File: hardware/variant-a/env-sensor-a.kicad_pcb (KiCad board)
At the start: 4 copper layers, 30 x 34 mm, 58 parts, among them J1 USB-C 16P, J2 JST-PH 2P, SW1 SW_PROV, U1 ESP32-C6-MINI-1-N4, U2 SHT45-AD1F, U3 TPS62840DLC, U4 BQ24074RGTR, U5 USBLC6-2SC6

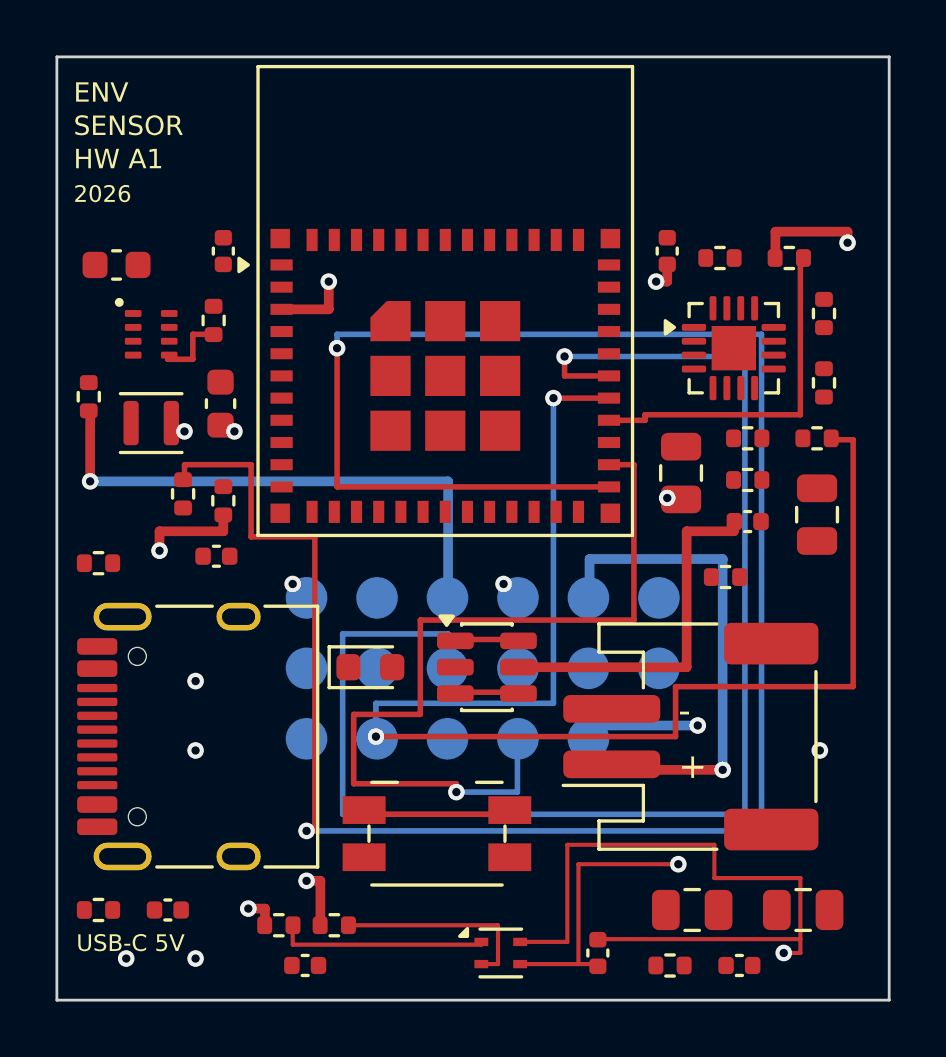
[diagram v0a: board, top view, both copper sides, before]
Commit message: chore(hw): regenerate both boards and previews after review fixes
Emit shared electrical corrections, validated routing and strengthened rules. Development allowances: A54/B58 unrouted and A6/B10 warnings per e584c6a; zero errors and parity differences. Preserve native KiCad SVG formatting. These are draft boards.
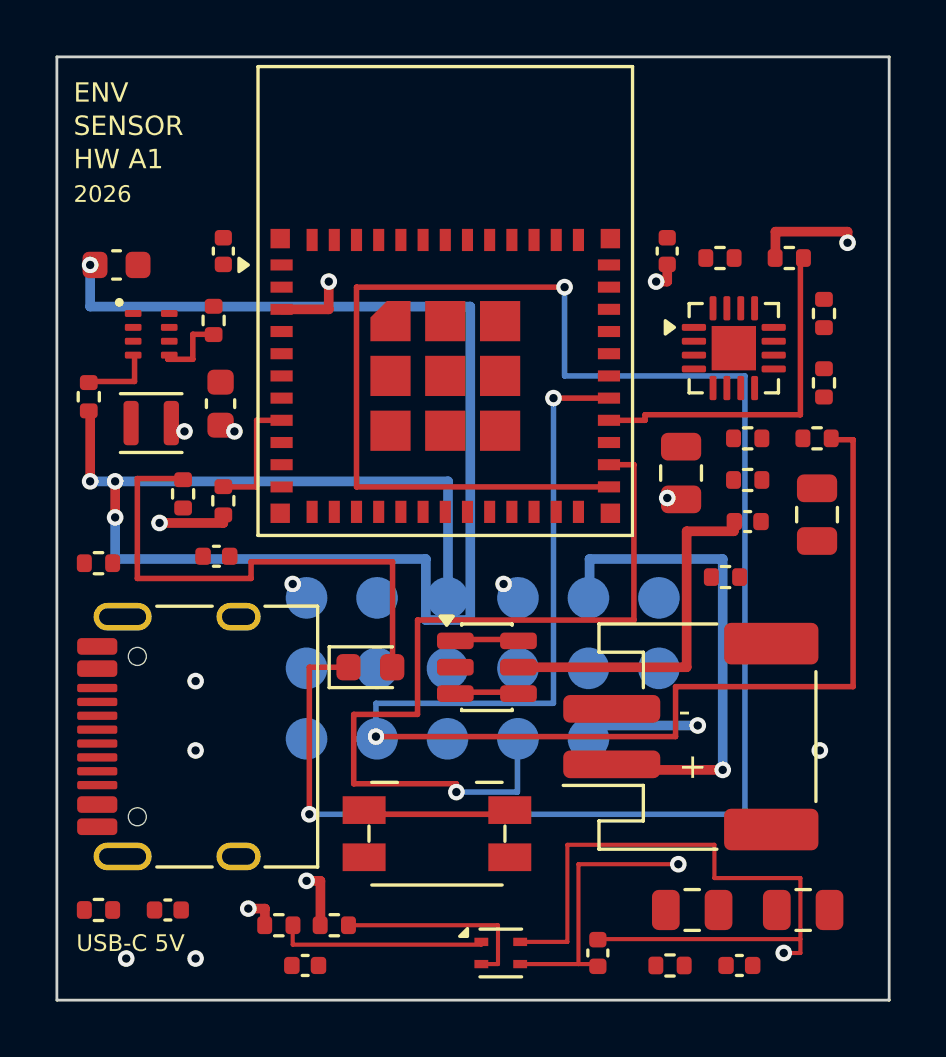
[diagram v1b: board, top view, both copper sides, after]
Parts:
- R6: value 52k3 1% -> 267k 1%
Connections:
- D1 pad 1: LED_A -> LED_N
- D1 pad 2: GND -> LED_A
- R2 pad 1: LED_A -> +3V0
- R2 pad 2: LED_N -> LED_A
- R5 pad 2: VSYS -> EN_REG
- U3 pad 4: VSYS -> EN_REG
- U4 pad 14: GND -> unconnected-(U4-TMR-Pad14)
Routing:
- net UART_RX: track 51.3 -> 0.00 mm, vias 1 -> 0
- net VSYS: track 19.7 -> 64.2 mm, vias 1 -> 4
- net LED_A: track 0.00 -> 18.9 mm
- net LED_N: track 83.6 -> 71.7 mm
- net EN: track 0.00 -> 4.50 mm
- net EN_REG: track 0.00 -> 2.60 mm
- net +3V0: track 27.6 -> 26.6 mm

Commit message: chore(hw): regenerate both variants for power architecture
Regenerate the shared schematic, both PCB layouts, symbol library, BOM, netlist, enclosure parameters, cost reports and floorplan previews from the updated electrical platform.

Record the reviewed KiCad 10 development budget: zero errors and parity differences, with 59 unrouted items on A and 60 on B. These artifacts remain non-release drafts.
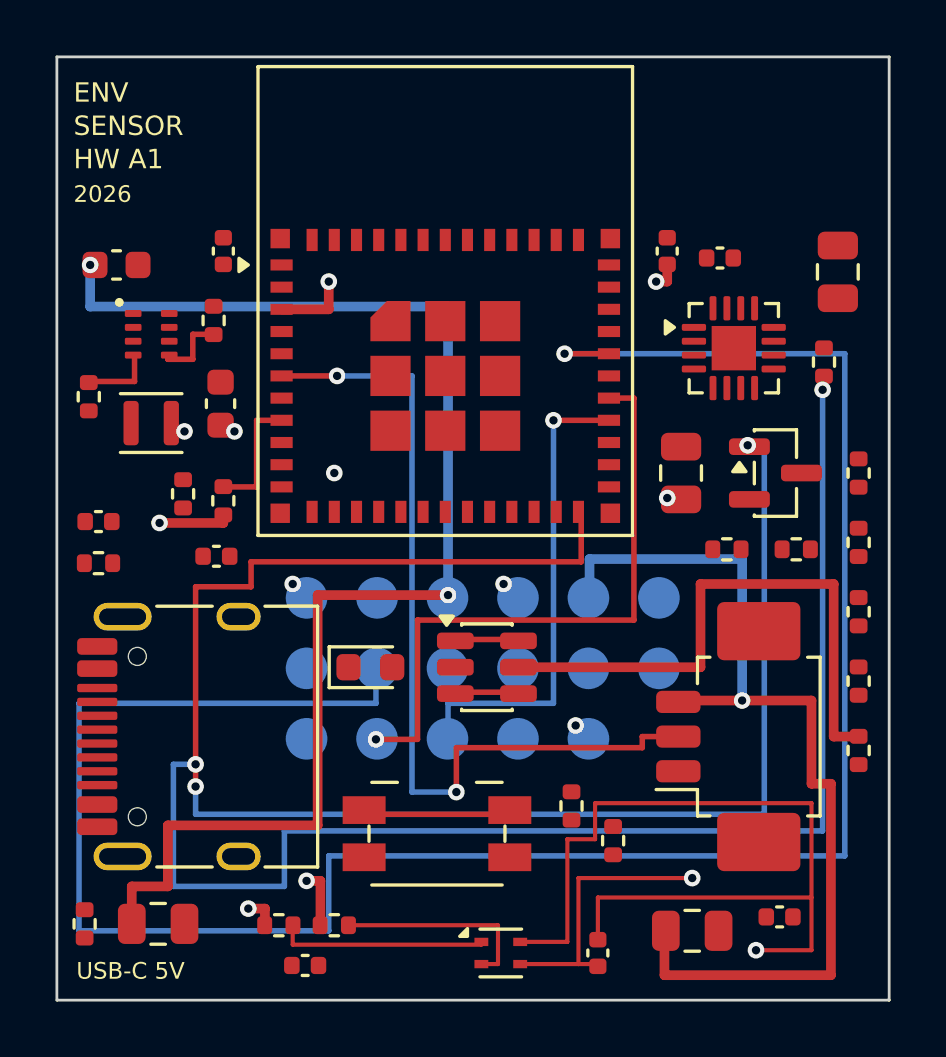
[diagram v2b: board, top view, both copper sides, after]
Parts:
- added Q1: 2N7002, sensorly:SOT-23, F.Cu at (125.9, 75.0)
- added R18: 47k 1%, sensorly:R_0402_1005Metric, F.Cu at (128.9, 85.0)
- J2: value JST-PH 2P -> Molex PicoBlade 3P; footprint sensorly:JST_PH_S2B-PH-SM4-TB_1x02-1MP_P2.00mm_Horizontal -> sensorly:Molex_PicoBlade_53261-0371_1x03-1MP_P1.25mm_Horizontal
- R11: value 3k09 1% -> 8k00 1%
- R13: value 3k57 1% -> 4k42 1%
- R7: value 10k 1% -> 100k 1%
- moved C10 19.3 mm to (103.7, 91.2)
- moved C14 14.2 mm to (101.5, 76.8)
- moved R9 10.6 mm to (128.9, 77.5), turned to 90 degrees
- moved R14 10.3 mm to (120.0, 88.2), turned to 90 degrees
- moved C12 9.55 mm to (123.9, 67.2)
- moved C9 8.78 mm to (128.2, 67.8)
- moved R11 8.56 mm to (126.7, 77.8), turned to 0 degrees
- moved R12 8.34 mm to (128.9, 80.0)
- moved R13 8.28 mm to (128.9, 82.5), turned to 90 degrees
- moved R15 6.76 mm to (118.5, 87.0), turned to 90 degrees
- moved R7 5.30 mm to (127.7, 71.0), turned to 90 degrees
- moved R10 5.15 mm to (124.2, 77.8)
- moved R8 4.19 mm to (128.9, 75.0), turned to 90 degrees
- moved C11 4.07 mm to (122.9, 91.5)
- moved C13 2.27 mm to (126.0, 91.0)
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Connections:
- J2 pad 1: VBAT -> GND
- J2 pad 2: GND -> PACK_TS
- J2 pad MP: GND -> unconnected-(J2-MountPin-PadMP)
- R7 pad 1: TS -> CHARGE_ENABLE
- R8 pad 1: VBUS -> USB_ISEL
- R8 pad 2: EN2 -> GND
- U1 pad 24: unconnected-(U1-IO18-Pad24) -> CHARGE_ENABLE
- U1 pad 27: unconnected-(U1-IO21-Pad27) -> USB_ISEL
- U1 pad 6: unconnected-(U1-IO3-Pad6) -> PACK_TS
- U4 pad 1: TS -> PACK_TS
- U4 pad 4: GND -> CHARGE_EN_N
- U4 pad 5: EN2 -> GND
- U4 pad 6: GND -> USB_ISEL
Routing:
- net CHARGE_ENABLE: track 0.00 -> 106.3 mm, vias 0 -> 4
- net UART_TX: track 0.00 -> 80.3 mm, vias 0 -> 1
- net LED_N: track 71.7 -> 0.00 mm, vias 2 -> 0
- net PACK_TS: track 0.00 -> 31.3 mm, vias 0 -> 2
- net TEST_MODE: track 30.6 -> 0.00 mm, vias 1 -> 0
- net CHG_N: track 49.3 -> 22.5 mm, vias 2 -> 1
- net LED_A: track 18.9 -> 0.00 mm
- net VBAT: track 18.0 -> 35.0 mm
- net VSYS: track 64.2 -> 48.2 mm, vias 4 -> 2
- net VBUS: track 13.0 -> 20.8 mm
- net PG_N: track 12.9 -> 17.3 mm, vias 0 -> 1
- net +3V0: track 26.6 -> 22.7 mm, vias 11 -> 10
- net GND: track 30.8 -> 34.0 mm, vias 8 -> 4
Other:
- board text added: "- T +"
- board text removed: "+"
- board text removed: "-"

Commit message: chore(hw): regenerate the controlled prototype checkpoint
Regenerate shared schematic/BOM/netlist, both PCB projects/rules and floorplan SVGs from the electrical, library and routing corrections in 3c343e2, 135b78b, d863f52, 7802bdf, 0852837 and 7206b19. Preserve R21 DNP and the common A/B electrical platform.

Fresh KiCad 10.0.6: zero ERC violations; both boards have zero DRC errors, warnings and schematic parity differences, with no ignored checks. Development routing exception: A59/B52 unconnected items remain, explicitly recorded in the budget; all old warning allowances are removed. Prototype and product manufacturing gates still require complete routing and real qualification evidence. Full committed-source pipeline follows before push.
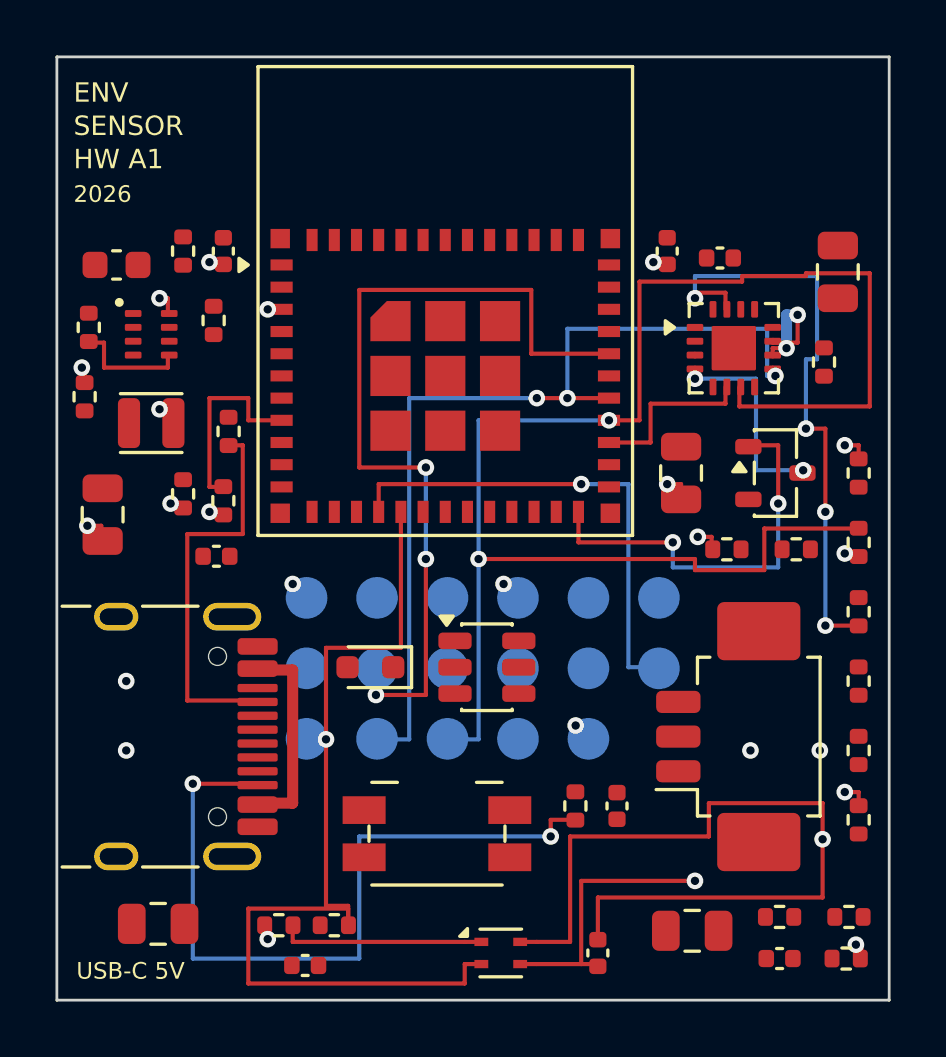
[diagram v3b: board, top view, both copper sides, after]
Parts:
- added R19: 100k 1%, sensorly:R_0402_1005Metric, F.Cu at (128.4, 92.5)
- added R20: 100k 1%, sensorly:R_0402_1005Metric, F.Cu at (128.9, 87.5)
- added R21: 0R, sensorly:R_0402_1005Metric, F.Cu at (104.5, 67.0)
- added R22: 10k 1%, sensorly:R_0402_1005Metric, F.Cu at (101.0, 72.2)
- C1: value 22uF/6.3V X5R -> 10uF/16V X5R
- C10, C11: value 10uF/6.3V X5R -> 10uF/16V X5R
- C3, C4: value 1uF/16V X7R -> 1uF/16V X5R
- C8: value 10uF/6.3V X5R -> 10uF/16V X5R; footprint sensorly:C_0603_1608Metric -> sensorly:C_0805_2012Metric
- D1: footprint sensorly:LED_0603_1608Metric -> sensorly:Kingbright_KP1608SGC
- L1: footprint sensorly:L_Murata_DFE201610P -> sensorly:L_Murata_DFE201612E
- Q1: footprint sensorly:SOT-23 -> sensorly:Onsemi_CASE318_SOT23
- R11: value 8k00 1% -> 8k06 1%
- TP10: value USB_DP -> USB_D_P
- TP11: value USB_DM -> USB_D_N
- TP7: value BTN_PROV -> BOOT_N
- U4: footprint sensorly:VQFN-16-1EP_3x3mm_P0.5mm_EP1.6x1.6mm -> sensorly:TI_RGT0016B_VQFN16_3x3mm
- U5: footprint sensorly:SOT-23-6 -> sensorly:ST_USBLC6_SOT23_6
- moved C14 21.3 mm to (120.2, 87.0), turned to 90 degrees
- moved R17 18.2 mm to (118.7, 87.0)
- moved R15 10.8 mm to (128.6, 91.0), turned to 0 degrees
- moved R16 6.68 mm to (106.2, 73.5), turned to 90 degrees
- moved R14 6.60 mm to (126.0, 91.0), turned to 0 degrees
- moved C8 5.84 mm to (101.7, 76.5)
- moved R5 5.27 mm to (105.7, 69.5)
- moved R6 4.51 mm to (101.2, 69.8)
- moved J1 2.31 mm to (103.2, 84.5), turned to 270 degrees
- moved C13 1.50 mm to (126.0, 92.5)
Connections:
- net USB_DM renamed USB_D_N
- net USB_DP renamed USB_D_P
- D1 pad 1: LED_N -> LED_A
- D1 pad 2: LED_A -> LED_N
- R8 pad 2: GND -> +3V0
- TP7 pad 1: BTN_PROV -> BOOT_N
- U1 pad 13: unconnected-(U1-IO1-Pad13) -> BTN_PROV
- U1 pad 19: unconnected-(U1-IO14-Pad19) -> USB_EN2
- U1 pad 22: unconnected-(U1-IO8-Pad22) -> BOOT_MODE_H
- U1 pad 23: BTN_PROV -> BOOT_N
- U1 pad 6: PACK_TS -> PACK_TS_SENSE
- U4 pad 5: GND -> USB_EN2
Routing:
- net CHARGE_ENABLE: track 106.3 -> 14.7 mm, vias 4 -> 2
- net UART_TX: track 80.3 -> 31.1 mm, vias 1 -> 3
- net VSYS: track 48.2 -> 4.40 mm
- net PG_N: track 17.3 -> 57.8 mm, vias 1 -> 2
- net VBAT: track 35.0 -> 0.10 mm, vias 1 -> 0
- net PACK_TS: track 31.3 -> 0.00 mm, vias 2 -> 0
- net SCL: track 7.40 -> 35.1 mm, vias 0 -> 1
- net CC2: track 0.00 -> 27.4 mm, vias 0 -> 2
- net ITERM: track 0.00 -> 22.0 mm, vias 0 -> 4
- net SDA: track 7.60 -> 25.1 mm, vias 0 -> 1
- net CC1: track 0.00 -> 14.2 mm
- net VBUS: track 20.8 -> 7.60 mm
- net CHG_N: track 22.5 -> 32.8 mm, vias 1 -> 3
- net CHARGE_EN_N: track 0.00 -> 7.60 mm, vias 0 -> 2
- net USB_ISEL: track 0.00 -> 6.20 mm
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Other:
- board text added: "J2 1- 2T 3+"
- board text removed: "- T +"

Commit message: build(boardgen): regenerate reviewed local power layouts
Regenerate both boards, rule areas, floorplan SVGs and enclosure parameters from 3109ac3. Preserve zero DRC errors/warnings/parity with A56/B49 unfinished connections; outputs remain draft engineering artifacts.
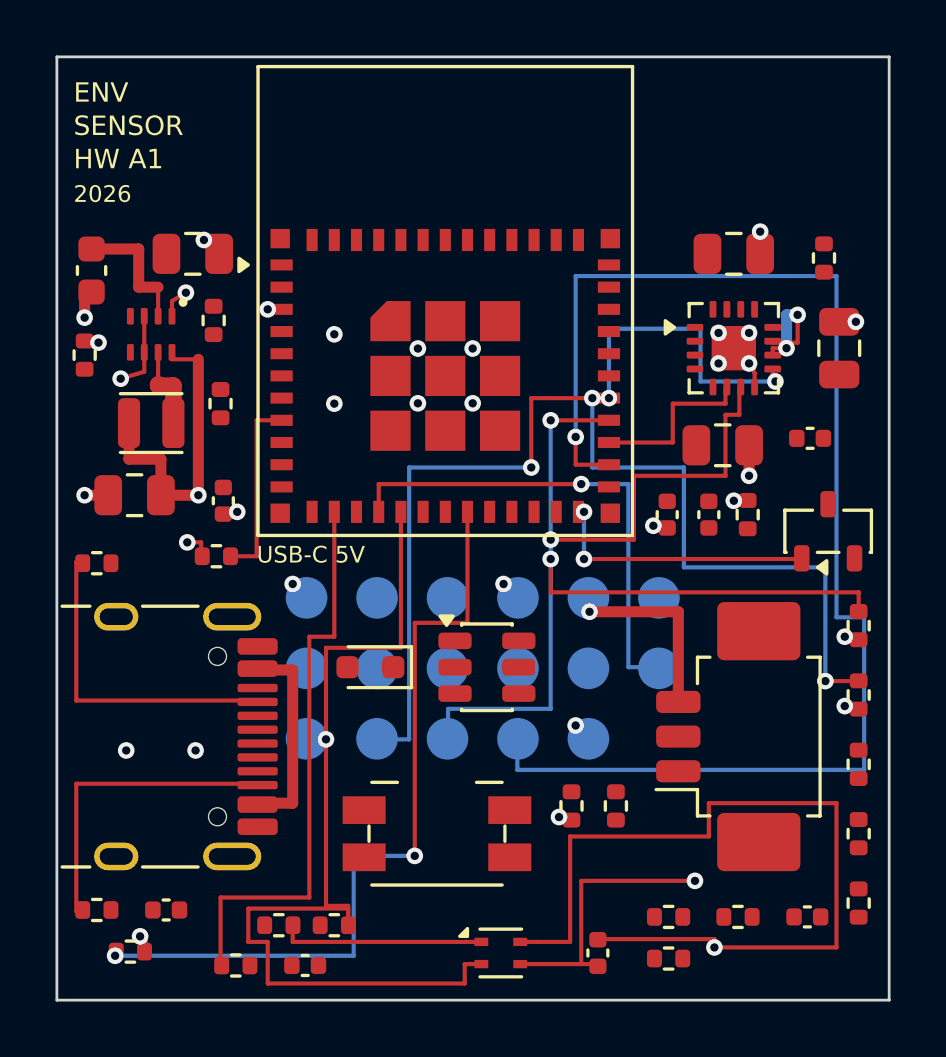
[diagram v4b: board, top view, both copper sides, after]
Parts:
- moved C10 32.1 mm to (128.2, 70.5), turned to 90 degrees
- moved R21 30.9 mm to (122.0, 92.5), turned to 0 degrees
- moved R20 26.7 mm to (102.7, 92.2), turned to 0 degrees
- moved R19 22.0 mm to (106.5, 92.8)
- moved C1 19.3 mm to (104.9, 67.1), turned to 180 degrees
- moved R2 18.0 mm to (118.5, 87.0)
- moved C4 17.8 mm to (123.5, 76.5), turned to 90 degrees
- moved R17 17.7 mm to (101.4, 90.8), turned to 0 degrees
- moved C11 17.5 mm to (124.0, 74.0)
- moved C14 16.7 mm to (103.9, 90.8), turned to 0 degrees
- moved R12 11.2 mm to (120.2, 87.0)
- moved C3 9.50 mm to (122.0, 76.5)
- moved C2 9.00 mm to (106.0, 76.0)
- moved R11 8.07 mm to (128.9, 85.5), turned to 90 degrees
- moved C12 7.27 mm to (127.2, 73.8)
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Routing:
- net TEST_MODE: track 0.10 -> 49.8 mm, vias 0 -> 1
- net UART_TX: track 31.1 -> 0.00 mm, vias 3 -> 0
- net USB_EN2: track 0.00 -> 28.7 mm, vias 0 -> 2
- net ITERM: track 22.0 -> 0.00 mm, vias 4 -> 0
- net BTN_PROV: track 0.00 -> 20.5 mm
- net CHG_N: track 32.8 -> 51.5 mm, vias 3 -> 5
- net CC2: track 27.4 -> 11.3 mm, vias 2 -> 0
- net PG_N: track 57.8 -> 42.6 mm, vias 2 -> 3
- net GND: track 30.9 -> 41.9 mm, vias 7 -> 22
- net CHARGE_EN_N: track 7.60 -> 0.00 mm, vias 2 -> 0
- net VBAT: track 0.10 -> 7.00 mm, vias 0 -> 1
- net +3V0: track 23.3 -> 29.5 mm, vias 18 -> 14
- net CHARGE_ENABLE: track 14.7 -> 9.50 mm
- net VSYS: track 4.40 -> 9.23 mm
- net VSET: track 4.20 -> 0.00 mm
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
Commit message: build(boardgen): regenerate local charger power routes
Regenerate both boards and model SVGs from the preceding charger-bypass source change. A47/B45 unconnected items remain explicitly recorded.
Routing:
- net EN: track 6.70 -> 62.4 mm, vias 0 -> 3
- net UART_TX: track 0.00 -> 40.1 mm, vias 0 -> 3
- net ILIM: track 0.00 -> 23.7 mm, vias 0 -> 2
- net LED_N: track 0.00 -> 21.3 mm, vias 0 -> 2
- net TEST_MODE: track 49.8 -> 29.6 mm
- net PACK_TS: track 0.00 -> 17.9 mm, vias 0 -> 2
- net CHARGE_ENABLE: track 9.50 -> 20.6 mm, vias 2 -> 4
- net CHG_N: track 51.5 -> 45.2 mm, vias 5 -> 4
- net VBUS: track 7.60 -> 11.3 mm
- net PG_N: track 42.6 -> 45.3 mm
- net USB_ISEL: track 6.20 -> 8.60 mm
- net USB_EN2: track 28.7 -> 29.9 mm
- net VBAT: track 7.00 -> 6.20 mm, vias 1 -> 0
- net VSYS: track 9.23 -> 9.22 mm, vias 2 -> 0

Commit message: build(boardgen): regenerate regulator control routing
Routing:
- net BOOT_MODE_H: track 0.40 -> 21.3 mm, vias 0 -> 4
- net VSET: track 0.00 -> 9.69 mm, vias 0 -> 2
- net EN_REG: track 0.00 -> 7.14 mm, vias 0 -> 2
- net +3V0: track 29.5 -> 28.9 mm, vias 14 -> 13
